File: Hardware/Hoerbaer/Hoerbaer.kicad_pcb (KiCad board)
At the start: 4 copper layers, 80 x 88 mm, 211 parts, among them J1 I2C, J10 Battery 1S Li-Ion, J12 Battery 1S Li-Ion, J13 JTAG, J14 Speaker_L, J15 Speaker_R, J16 USB2_UART, J17 RST_BOOT, J2 DISPLAY, J3 Micro_SD_Card_Det1, J4 USB1, J5 ENCODER, J6 PAW_A, J7 PAW_B, J8 PAW_C, J9 PAW_D, Q1 DMG3415UQ-7, Q5 S8050, Q6 S8050, SW1 RESET, SW2 PROG, U1 ESP32 S3 MINI, U10 TAS5805M, U11 CH343P, U12 MAX17048G, U13 TPS61288, U2 PCF8574APWR, U3 PCF8574APWR, U4 PCF8574APWR, U5 TLC59108xPW, U6 TLC59108xPW, U7 TLC59108xPW, U8 MCP73831T-2ACI/OT (4.2V), U9 TPS63001

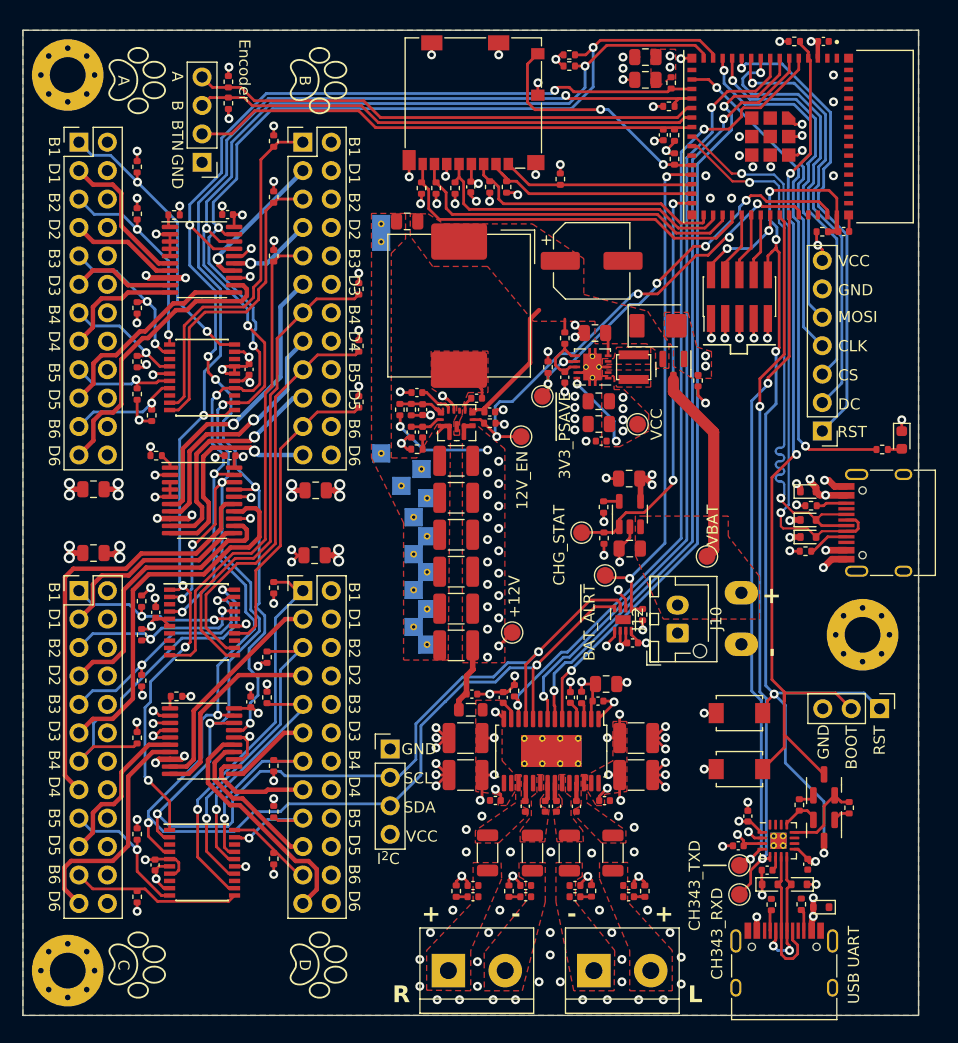
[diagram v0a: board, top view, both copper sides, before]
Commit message: Added an additional connector. And silk screen designs.
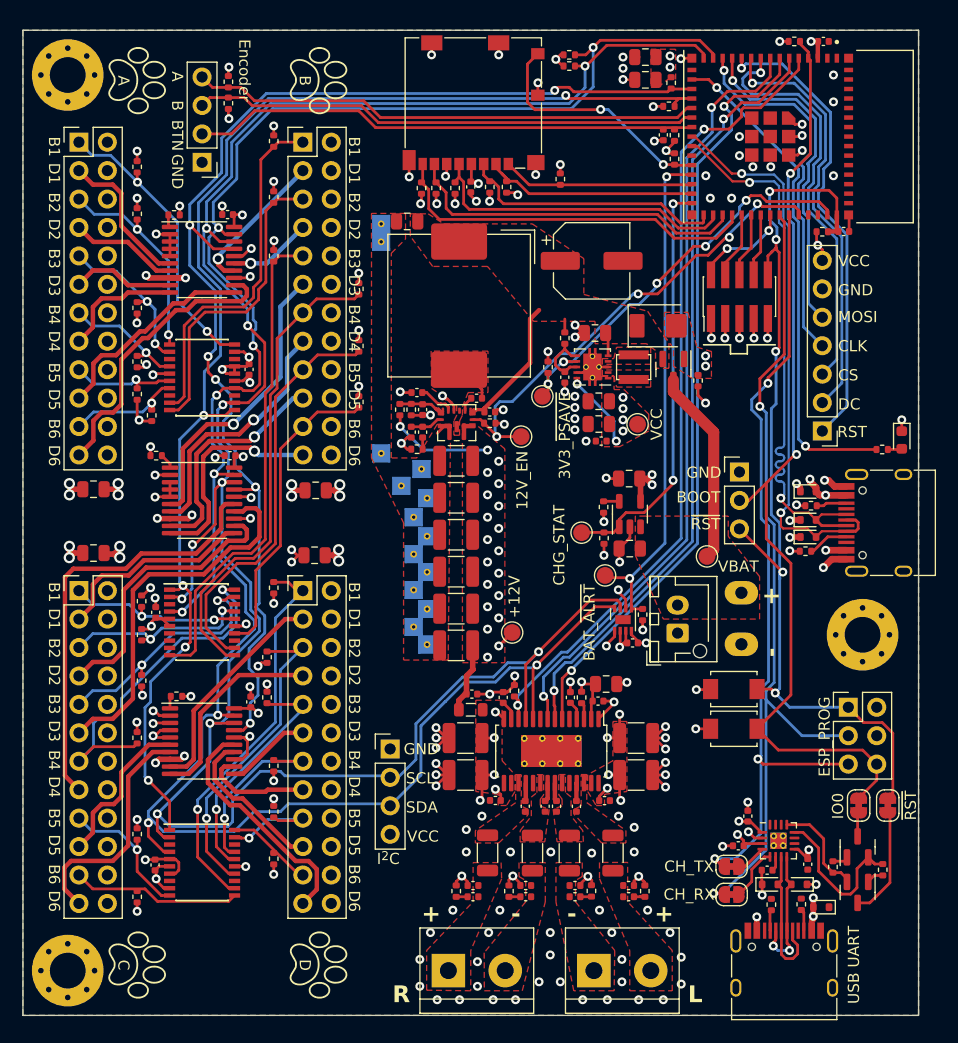
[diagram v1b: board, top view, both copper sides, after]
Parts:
- removed TP2: CH343_RXD, TestPoint:TestPoint_Pad_D1.5mm
- removed TP3: CH343_TXD, TestPoint:TestPoint_Pad_D1.5mm
- added ESP_PROG: UART, Connector_PinHeader_2.54mm:PinHeader_2x03_P2.54mm_Vertical, F.Cu at (133.7, 120.5)
- added JP1: CH_TX, Jumper:SolderJumper-2_P1.3mm_Bridged_RoundedPad1.0x1.5mm, F.Cu at (123.3, 134.7)
- added JP2: CH_RX, Jumper:SolderJumper-2_P1.3mm_Bridged_RoundedPad1.0x1.5mm, F.Cu at (123.3, 137.2)
- added JP3: ~{RST}, Jumper:SolderJumper-2_P1.3mm_Bridged_RoundedPad1.0x1.5mm, F.Cu at (137.2, 129.2)
- added JP4: IO0, Jumper:SolderJumper-2_P1.3mm_Bridged_RoundedPad1.0x1.5mm, F.Cu at (134.7, 129.2)
- added REF**: OSHW-Logo2_9.8x8mm_SilkScreen, Symbol:OSHW-Logo2_9.8x8mm_SilkScreen, B.Cu at (127.0, 67.0)
- moved J17 24.6 mm to (124.0, 99.5), turned to 0 degrees
- moved R69 6.30 mm to (136.8, 135.0)
- moved R70 6.30 mm to (132.3, 134.7)
- moved Q5 6.30 mm to (134.6, 137.0)
- moved Q6 6.30 mm to (134.6, 132.9)
- moved SW2 3.63 mm to (123.5, 122.4)
- moved SW1 2.21 mm to (123.5, 118.8)
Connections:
- J17 pad 1: /MCU_~{RST} -> GND
- J17 pad 3: GND -> /MCU_~{RST}
- Q5 pad 3: /MCU_~{RST} -> /USB_UART/USB_UART_MCU_~{RST}_CHIP
- Q6 pad 3: /MCU_IO0 -> /USB_UART/USB_UART_MCU_GPIO0_CHIP
- U11 pad 4: /MCU_RXD -> /USB_UART/USB_UART_TXD_CHIP
- U11 pad 5: /MCU_TXD -> /USB_UART/USB_UART_RXD_CHIP
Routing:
- net /MCU_TXD: track 63.7 -> 74.6 mm
- net /MCU_RXD: track 62.3 -> 72.4 mm, vias 2 -> 3
- net /USB_UART/USB_UART_MCU_~{RST}_CHIP: track 0.00 -> 9.97 mm
- net Net-(Q6-E): track 7.50 -> 14.0 mm
- net Net-(Q5-E): track 3.48 -> 8.67 mm
- net /USB_UART/USB_UART_RXD_CHIP: track 0.00 -> 4.81 mm
- net /MCU_IO0: track 81.1 -> 85.1 mm
- net /MCU_~{RST}: track 88.5 -> 85.0 mm
- net /USB_UART/USB_UART_TXD_CHIP: track 0.00 -> 2.73 mm
- net /USB_UART/USB_UART_MCU_GPIO0_CHIP: track 0.00 -> 1.87 mm
- net /USB_UART/USB2_VBUS: track 28.9 -> 29.7 mm
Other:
- board text added: "Drachosaurus Designs"
- board text added: "Hör Bär"
- board text added: "https://github.com/drachosaurus/hoerbaer"
- board text added: "~{RST}"
